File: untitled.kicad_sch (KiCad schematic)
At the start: 12 parts, among them U5 EUP3489WIR1

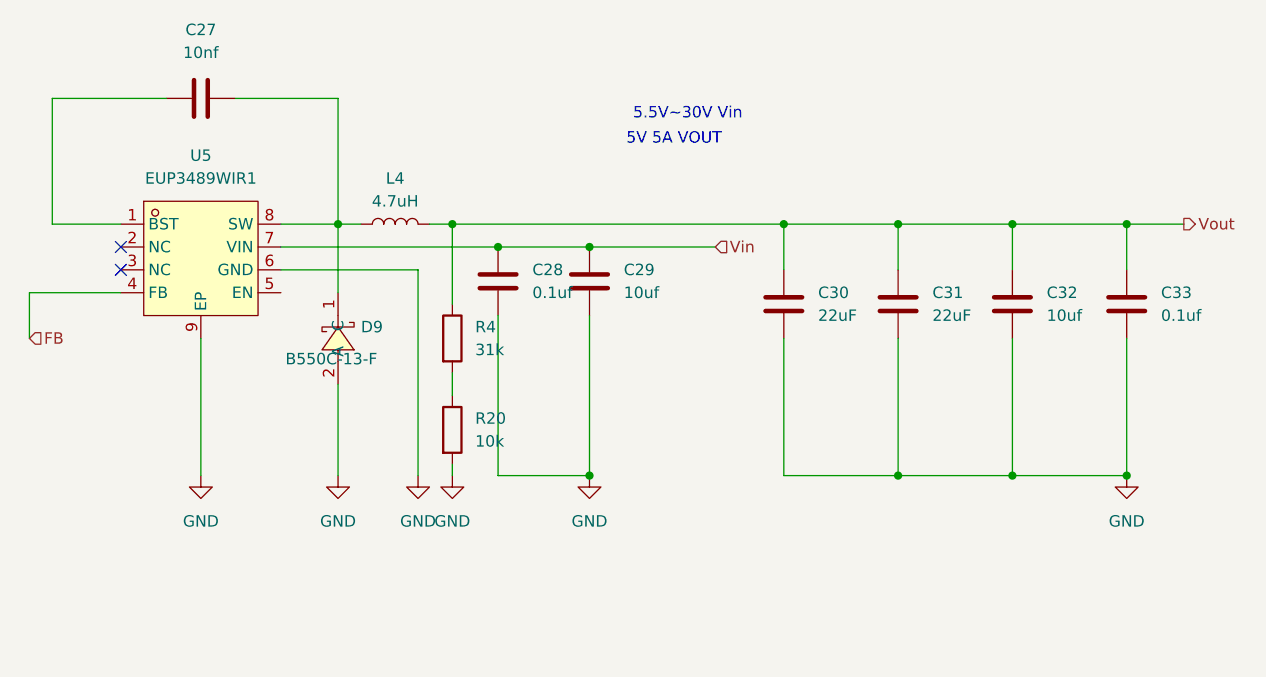
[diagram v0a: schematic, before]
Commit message: finished getting footprints and started layout
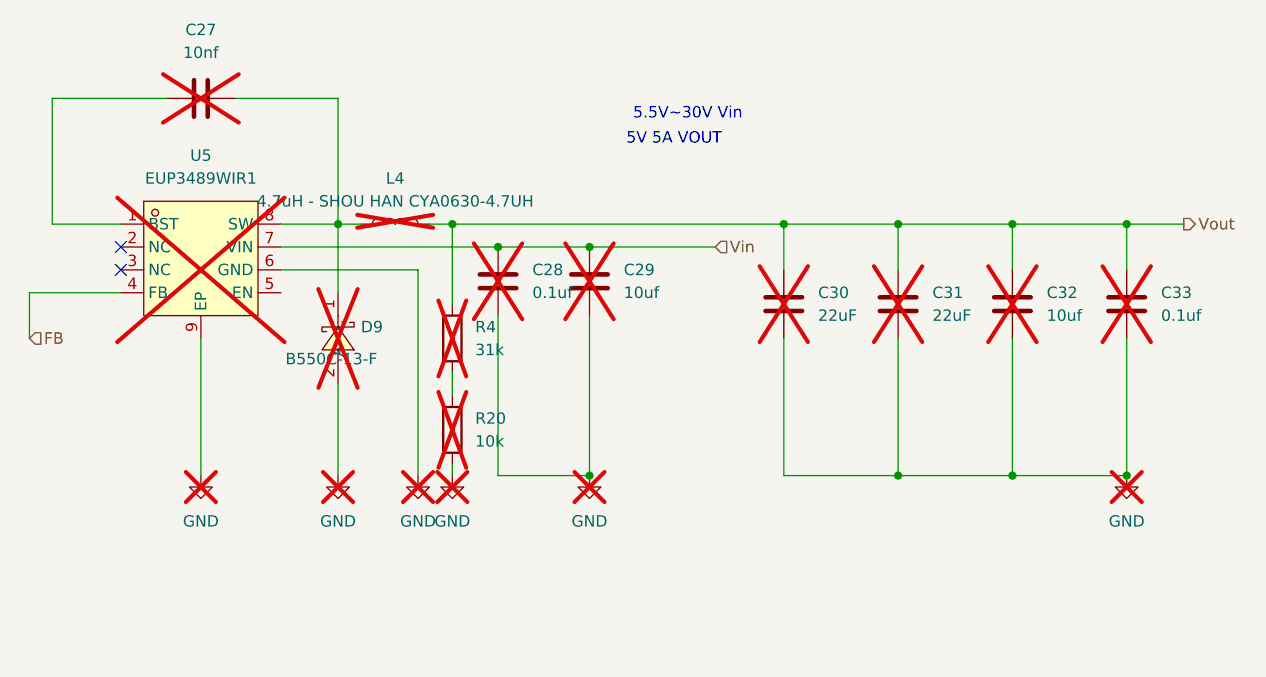
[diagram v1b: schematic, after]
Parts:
- C27, C28, C33: footprint (none) -> Capacitor_SMD:C_0603_1608Metric_Pad1.08x0.95mm_HandSolder; now not fitted
- C29, C30, C31, C32: footprint (none) -> Capacitor_SMD:C_0805_2012Metric_Pad1.18x1.45mm_HandSolder; now not fitted
- D9, U5: now not fitted
- L4: value 4.7uH -> 4.7uH - SHOU HAN CYA0630-4.7UH; footprint (none) -> easyeda2kicad:IND-SMD_L7.2-W6.6_GPSR07X0; now not fitted
- R20, R4: footprint (none) -> Resistor_SMD:R_0603_1608Metric_Pad0.98x0.95mm_HandSolder; now not fitted
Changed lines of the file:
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@@
 		(in_bom yes)
 		(on_board yes)
-		(dnp no)
+		(dnp yes)
 		(fields_autoplaced yes)
 		(property "Reference" "C33"
@@
 			)
 		)
-		(property "Footprint" ""
+		(property "Footprint" "Capacitor_SMD:C_0603_1608Metric_Pad1.08x0.95mm_HandSolder"
 			(at 272.7452 81.28 0)
 			(effects
@@
 		(in_bom yes)
 		(on_board yes)
-		(dnp no)
+		(dnp yes)
 		(fields_autoplaced yes)
 		(property "Reference" "U5"
@@
 		(in_bom yes)
 		(on_board yes)
-		(dnp no)
+		(dnp yes)
 		(fields_autoplaced yes)
 		(property "Reference" "C29"
@@
 			)
 		)
-		(property "Footprint" ""
+		(property "Footprint" "Capacitor_SMD:C_0805_2012Metric_Pad1.18x1.45mm_HandSolder"
 			(at 213.0552 78.74 0)
 			(effects
@@
 		(in_bom yes)
 		(on_board yes)
-		(dnp no)
+		(dnp yes)
 		(fields_autoplaced yes)
 		(property "Reference" "C32"
@@
 			)
 		)
-		(property "Footprint" ""
+		(property "Footprint" "Capacitor_SMD:C_0805_2012Metric_Pad1.18x1.45mm_HandSolder"
 			(at 260.0452 81.28 0)
 			(effects
@@
 		(in_bom yes)
 		(on_board yes)
-		(dnp no)
+		(dnp yes)
 		(fields_autoplaced yes)
 		(property "Reference" "#PWR031"
@@
 		(in_bom yes)
 		(on_board yes)
-		(dnp no)
+		(dnp yes)
 		(fields_autoplaced yes)
 		(property "Reference" "C27"
@@
 			)
 		)
-		(property "Footprint" ""
+		(property "Footprint" "Capacitor_SMD:C_0603_1608Metric_Pad1.08x0.95mm_HandSolder"
 			(at 172.72 53.6448 0)
 			(effects
@@
 		(in_bom yes)
 		(on_board yes)
-		(dnp no)
+		(dnp yes)
 		(fields_autoplaced yes)
 		(property "Reference" "#PWR032"
@@
 		(in_bom yes)
 		(on_board yes)
-		(dnp no)
+		(dnp yes)
 		(fields_autoplaced yes)
 		(property "Reference" "C28"
@@
 			)
 		)
-		(property "Footprint" ""
+		(property "Footprint" "Capacitor_SMD:C_0603_1608Metric_Pad1.08x0.95mm_HandSolder"
 			(at 202.8952 78.74 0)
 			(effects
@@
 		(in_bom yes)
 		(on_board yes)
-		(dnp no)
+		(dnp yes)
 		(fields_autoplaced yes)
 		(property "Reference" "L4"
@@
 			)
 		)
-		(property "Value" "4.7uH"
+		(property "Value" "4.7uH - SHOU HAN CYA0630-4.7UH"
 			(at 190.5 66.04 90)
 			(effects
@@
 			)
 		)
-		(property "Footprint" ""
+		(property "Footprint" "easyeda2kicad:IND-SMD_L7.2-W6.6_GPSR07X0"
 			(at 190.5 68.58 0)
 			(effects
@@
 		(in_bom yes)
 		(on_board yes)
-		(dnp no)
+		(dnp yes)
 		(fields_autoplaced yes)
 		(property "Reference" "R20"
@@
 			)
 		)
-		(property "Footprint" ""
+		(property "Footprint" "Resistor_SMD:R_0603_1608Metric_Pad0.98x0.95mm_HandSolder"
 			(at 195.072 91.44 90)
 			(effects
@@
 		(in_bom yes)
 		(on_board yes)
-		(dnp no)
+		(dnp yes)
 		(fields_autoplaced yes)
 		(property "Reference" "#PWR034"
@@
 		(in_bom yes)
 		(on_board yes)
-		(dnp no)
+		(dnp yes)
 		(fields_autoplaced yes)
 		(property "Reference" "#PWR033"
@@
 		(in_bom yes)
 		(on_board yes)
-		(dnp no)
+		(dnp yes)
 		(fields_autoplaced yes)
 		(property "Reference" "#PWR035"
@@
 		(in_bom yes)
 		(on_board yes)
-		(dnp no)
+		(dnp yes)
 		(fields_autoplaced yes)
 		(property "Reference" "C30"
@@
 			)
 		)
-		(property "Footprint" ""
+		(property "Footprint" "Capacitor_SMD:C_0805_2012Metric_Pad1.18x1.45mm_HandSolder"
 			(at 234.6452 81.28 0)
 			(effects
@@
 		(in_bom yes)
 		(on_board yes)
-		(dnp no)
+		(dnp yes)
 		(fields_autoplaced yes)
 		(property "Reference" "R4"
@@
 			)
 		)
-		(property "Footprint" ""
+		(property "Footprint" "Resistor_SMD:R_0603_1608Metric_Pad0.98x0.95mm_HandSolder"
 			(at 195.072 81.28 90)
 			(effects
@@
 		(in_bom yes)
 		(on_board yes)
-		(dnp no)
+		(dnp yes)
 		(fields_autoplaced yes)
 		(property "Reference" "#PWR030"
@@
 		(in_bom yes)
 		(on_board yes)
-		(dnp no)
+		(dnp yes)
 		(property "Reference" "D9"
 			(at 186.69 80.0099 90)
@@
 		(in_bom yes)
 		(on_board yes)
-		(dnp no)
+		(dnp yes)
 		(fields_autoplaced yes)
 		(property "Reference" "C31"
@@
 			)
 		)
-		(property "Footprint" ""
+		(property "Footprint" "Capacitor_SMD:C_0805_2012Metric_Pad1.18x1.45mm_HandSolder"
 			(at 247.3452 81.28 0)
 			(effects

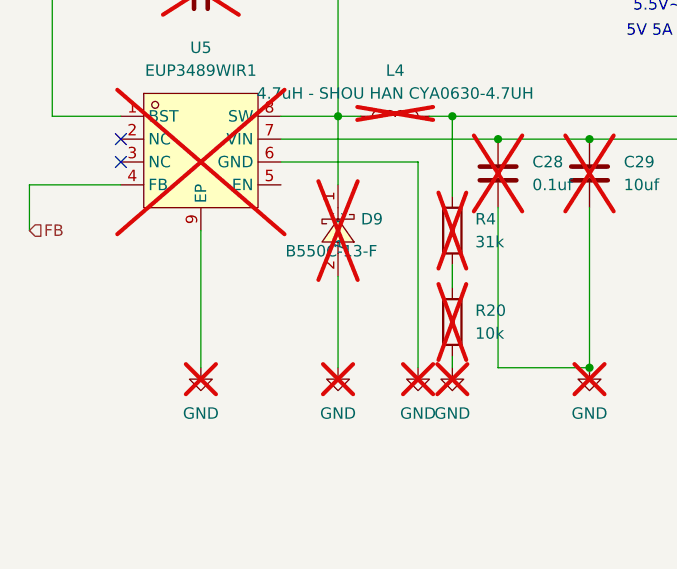
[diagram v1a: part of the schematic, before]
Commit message: routing and layout done except spacing and final power route
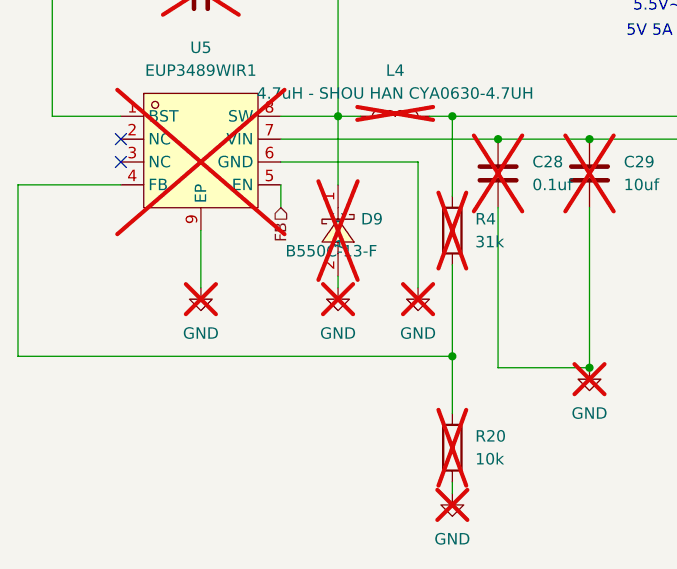
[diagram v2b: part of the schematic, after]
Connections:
- net FB: now also U5.5 (EN); no longer U5.4 (FB)
- net at R20.1, R4.2: now also U5.4 (FB)
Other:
- moved on the sheet: R20
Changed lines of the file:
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@@
+	)
+	(junction
+		(at 196.85 95.25)
+		(diameter 0)
+		(color 0 0 0 0)
 	)
 	(junction
@@
 	(wire
 		(pts
-			(xy 149.86 76.2) (xy 149.86 81.28)
-		)
-		(stroke
-			(width 0)
-			(type default)
-		)
-	)
-	(wire
-		(pts
 			(xy 233.68 73.66) (xy 233.68 68.58)
 		)
@@
 	(wire
 		(pts
+			(xy 148.59 76.2) (xy 148.59 95.25)
+		)
+		(stroke
+			(width 0)
+			(type default)
+		)
+	)
+	(wire
+		(pts
 			(xy 233.68 68.58) (xy 246.38 68.58)
 		)
@@
 	(wire
 		(pts
-			(xy 193.04 73.66) (xy 193.04 96.52)
+			(xy 193.04 73.66) (xy 193.04 87.63)
 		)
 		(stroke
@@
 	(wire
 		(pts
-			(xy 184.15 86.36) (xy 184.15 96.52)
+			(xy 184.15 86.36) (xy 184.15 87.63)
 		)
 		(stroke
@@
 	(wire
 		(pts
+			(xy 177.8 76.2) (xy 177.8 78.74)
+		)
+		(stroke
+			(width 0)
+			(type default)
+		)
+	)
+	(wire
+		(pts
 			(xy 152.4 54.61) (xy 165.1 54.61)
 		)
@@
 	(wire
 		(pts
-			(xy 196.85 95.25) (xy 196.85 96.52)
+			(xy 196.85 109.22) (xy 196.85 110.49)
 		)
 		(stroke
@@
 	(wire
 		(pts
-			(xy 196.85 85.09) (xy 196.85 87.63)
+			(xy 196.85 85.09) (xy 196.85 95.25)
 		)
 		(stroke
@@
 	(wire
 		(pts
-			(xy 160.02 76.2) (xy 149.86 76.2)
+			(xy 148.59 95.25) (xy 196.85 95.25)
+		)
+		(stroke
+			(width 0)
+			(type default)
+		)
+	)
+	(wire
+		(pts
+			(xy 160.02 76.2) (xy 148.59 76.2)
 		)
 		(stroke
@@
 	(wire
 		(pts
+			(xy 196.85 95.25) (xy 196.85 101.6)
+		)
+		(stroke
+			(width 0)
+			(type default)
+		)
+	)
+	(wire
+		(pts
 			(xy 212.09 71.12) (xy 226.06 71.12)
 		)
@@
 	(wire
 		(pts
-			(xy 168.91 81.28) (xy 168.91 96.52)
+			(xy 168.91 81.28) (xy 168.91 87.63)
 		)
 		(stroke
@@
 	(hierarchical_label "FB"
 		(shape input)
-		(at 149.86 81.28 0)
+		(at 177.8 78.74 270)
 		(effects
 			(font
 				(size 1.27 1.27)
 			)
-			(justify left)
+			(justify right)
 		)
 	)
@@
 	(symbol
 		(lib_id "power:GND")
-		(at 184.15 96.52 0)
+		(at 184.15 87.63 0)
 		(unit 1)
 		(exclude_from_sim no)
@@
 		(fields_autoplaced yes)
 		(property "Reference" "#PWR031"
-			(at 184.15 102.87 0)
+			(at 184.15 93.98 0)
 			(effects
 				(font
@@
 		)
 		(property "Value" "GND"
-			(at 184.15 101.6 0)
+			(at 184.15 92.71 0)
 			(effects
 				(font
@@
 		)
 		(property "Footprint" ""
-			(at 184.15 96.52 0)
+			(at 184.15 87.63 0)
 			(effects
 				(font
@@
 		)
 		(property "Datasheet" ""
-			(at 184.15 96.52 0)
+			(at 184.15 87.63 0)
 			(effects
 				(font
@@
 		)
 		(property "Description" "Power symbol creates a global label with name \"GND\" , ground"
-			(at 184.15 96.52 0)
+			(at 184.15 87.63 0)
 			(effects
 				(font
@@
 	(symbol
 		(lib_id "power:GND")
-		(at 193.04 96.52 0)
+		(at 193.04 87.63 0)
 		(unit 1)
 		(exclude_from_sim no)
@@
 		(fields_autoplaced yes)
 		(property "Reference" "#PWR032"
-			(at 193.04 102.87 0)
+			(at 193.04 93.98 0)
 			(effects
 				(font
@@
 		)
 		(property "Value" "GND"
-			(at 193.04 101.6 0)
+			(at 193.04 92.71 0)
 			(effects
 				(font
@@
 		)
 		(property "Footprint" ""
-			(at 193.04 96.52 0)
+			(at 193.04 87.63 0)
 			(effects
 				(font
@@
 		)
 		(property "Datasheet" ""
-			(at 193.04 96.52 0)
+			(at 193.04 87.63 0)
 			(effects
 				(font
@@
 		)
 		(property "Description" "Power symbol creates a global label with name \"GND\" , ground"
-			(at 193.04 96.52 0)
+			(at 193.04 87.63 0)
 			(effects
 				(font
@@
 	(symbol
 		(lib_id "Device:R")
-		(at 196.85 91.44 0)
+		(at 196.85 105.41 0)
 		(unit 1)
 		(exclude_from_sim no)
@@
 		(fields_autoplaced yes)
 		(property "Reference" "R20"
-			(at 199.39 90.1699 0)
+			(at 199.39 104.1399 0)
 			(effects
 				(font
@@
 		)
 		(property "Value" "10k"
-			(at 199.39 92.7099 0)
+			(at 199.39 106.6799 0)
 			(effects
 				(font
@@
 		)
 		(property "Footprint" "Resistor_SMD:R_0603_1608Metric_Pad0.98x0.95mm_HandSolder"
-			(at 195.072 91.44 90)
+			(at 195.072 105.41 90)
 			(effects
 				(font
@@
 		)
 		(property "Datasheet" "~"
-			(at 196.85 91.44 0)
+			(at 196.85 105.41 0)
 			(effects
 				(font
@@
 		)
 		(property "Description" "Resistor"
-			(at 196.85 91.44 0)
+			(at 196.85 105.41 0)
 			(effects
 				(font
@@
 	(symbol
 		(lib_id "power:GND")
-		(at 196.85 96.52 0)
+		(at 196.85 110.49 0)
 		(unit 1)
 		(exclude_from_sim no)
@@
 		(fields_autoplaced yes)
 		(property "Reference" "#PWR033"
-			(at 196.85 102.87 0)
+			(at 196.85 116.84 0)
 			(effects
 				(font
@@
 		)
 		(property "Value" "GND"
-			(at 196.85 101.6 0)
+			(at 196.85 115.57 0)
 			(effects
 				(font
@@
 		)
 		(property "Footprint" ""
-			(at 196.85 96.52 0)
+			(at 196.85 110.49 0)
 			(effects
 				(font
@@
 		)
 		(property "Datasheet" ""
-			(at 196.85 96.52 0)
+			(at 196.85 110.49 0)
 			(effects
 				(font
@@
 		)
 		(property "Description" "Power symbol creates a global label with name \"GND\" , ground"
-			(at 196.85 96.52 0)
+			(at 196.85 110.49 0)
 			(effects
 				(font
@@
 	(symbol
 		(lib_id "power:GND")
-		(at 168.91 96.52 0)
+		(at 168.91 87.63 0)
 		(unit 1)
 		(exclude_from_sim no)
@@
 		(fields_autoplaced yes)
 		(property "Reference" "#PWR030"
-			(at 168.91 102.87 0)
+			(at 168.91 93.98 0)
 			(effects
 				(font
@@
 		)
 		(property "Value" "GND"
-			(at 168.91 101.6 0)
+			(at 168.91 92.71 0)
 			(effects
 				(font
@@
 		)
 		(property "Footprint" ""
-			(at 168.91 96.52 0)
+			(at 168.91 87.63 0)
 			(effects
 				(font
@@
 		)
 		(property "Datasheet" ""
-			(at 168.91 96.52 0)
+			(at 168.91 87.63 0)
 			(effects
 				(font
@@
 		)
 		(property "Description" "Power symbol creates a global label with name \"GND\" , ground"
-			(at 168.91 96.52 0)
-			(effects
-				(font
+			(at 168.91 87.63 0)
+			(effects
+				(font
